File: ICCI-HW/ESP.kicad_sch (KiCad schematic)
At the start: 45 parts, among them J501 JTAG, SW501 SW_BOOT, SW502 SW_RST, SW503 SW_LOG_SD_EN, SW504 SW_RST_PROV, SW505 SW_RGB_CHRG, SW506 SW_SLEEP, U501 ESP32-WROVER-IE/E, U502 SX1503I091TRT

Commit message: hw: updates
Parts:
- added C512, C513, C516: 4.7u, Capacitor_SMD:C_0603_1608Metric, symbol Device:C
- added C514, C515, C517: 100n, Capacitor_SMD:C_0603_1608Metric, symbol Device:C
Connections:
- net +3V3: now also C512.1, C513.1, C514.1, C515.1, C516.1, C517.1
- net GND: now also C512.2, C513.2, C514.2, C515.2, C516.2, C517.2

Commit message: hw: updates
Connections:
- net RXD: no longer R512.2, U501.34 (RXD0)
- net TXD: no longer R511.1, U501.35 (TXD0)
- new net RXDR: R512.2, U501.34 (RXD0)
- new net TXDR: R511.1, U501.35 (TXD0)
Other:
- note added: "BOOT"
- note added: "RST"
- note added: "VSPI_D"
- note added: "VSPI_Q"
- moved on the sheet: C502, C504, C507, C508, C509, D501, D502, R505, R506, R507, R511, R512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

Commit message: start layout
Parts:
- removed J501: JTAG, Connector_PinHeader_2.54mm:PinHeader_1x04_P2.54mm_Vertical, symbol Connector_Generic:Conn_01x04
- removed TP506: TP_CLK/TP, TestPoint:TestPoint_Plated_Hole_D2.0mm, symbol Connector:TestPoint
- added J501: JTAG, ICCI-LIB:JST_B6B-XH-A, symbol Connector:Conn_01x06_Male
- added JP501, JP502, JP503: SolderJumper_3_Bridged12, Jumper:SolderJumper-3_P1.3mm_Open_RoundedPad1.0x1.5mm_NumberLabels, symbol Jumper:SolderJumper_3_Bridged12
- TP501, TP502, TP503, TP504, TP505, TP507, TP508: footprint TestPoint:TestPoint_Plated_Hole_D2.0mm -> TestPoint:TestPoint_THTPad_D1.5mm_Drill0.7mm
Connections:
- net +3V3: now also J501.6 (Pin_6)
- net GND: now also J501.1 (Pin_1)
- net GPS_EXTINT: now also JP503.3 (B); no longer U502.20 (I/O[13])
- net GPS_TP: now also JP501.3 (B); no longer U502.23 (I/O[15])
- net TCK: now also J501.4 (Pin_4)
- net TDI: now also J501.2 (Pin_2)
- net TDO: now also J501.3 (Pin_3)
- net TMS: now also J501.5 (Pin_5)
- net ~{GPS_RESET}: now also JP502.3 (B); no longer U502.22 (I/O[14])
- new net: JP501.2 (C), U502.23 (I/O[15])
- new net: JP503.2 (C), U502.20 (I/O[13])
- new net: JP502.2 (C), U502.22 (I/O[14])
- new net RTC_CLKOUT: JP501.1 (A)
- new net ~{RTC_INT}: JP503.1 (A)
- new net ~{RTC_RST}: JP502.1 (A)
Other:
- note added: "Solder Jumpers Pos. 1-2 if RTC mounted, 3-2 if GPS mounted."
- moved on the sheet: TP503

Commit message: layout PCB V1.0
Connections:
- net ~{EXP_RESET} renamed ~{EXP_RST}
- net ~{GPS_RESET} renamed ~{GPS_RST}
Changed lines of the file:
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@@
     (title "ESP")
     (date "2022-07-14")
-    (rev "BETA")
+    (rev "1.0")
     (company "Simone Tollardo")
   )
@@
     (effects (font (size 1.27 1.27)) (justify left bottom))
   )
-  (label "~{EXP_RESET}" (at 212.725 62.865 180)
+  (label "~{EXP_RST}" (at 212.725 62.865 180)
     (effects (font (size 1.27 1.27)) (justify right bottom))
   )
@@
     (effects (font (size 1.27 1.27)) (justify right bottom))
   )
-  (label "~{EXP_RESET}" (at 172.466 59.69 180)
+  (label "~{EXP_RST}" (at 172.466 59.69 180)
     (effects (font (size 1.27 1.27)) (justify right bottom))
   )
@@
     (effects (font (size 1.27 1.27)) (justify right))
   )
-  (hierarchical_label "~{GPS_RESET}" (shape output) (at 222.885 29.21 180)
+  (hierarchical_label "~{GPS_RST}" (shape output) (at 222.885 29.21 180)
     (effects (font (size 1.27 1.27)) (justify right))
   )

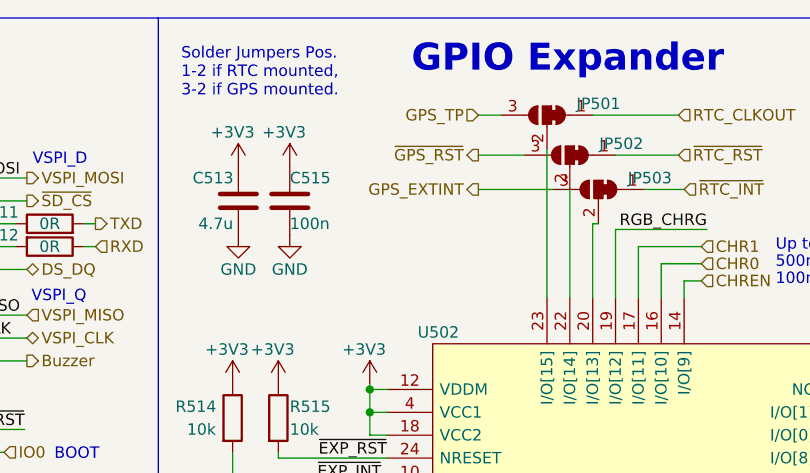
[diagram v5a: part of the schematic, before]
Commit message: hw: fix missing contact from SYS to SYSA on MAX77960
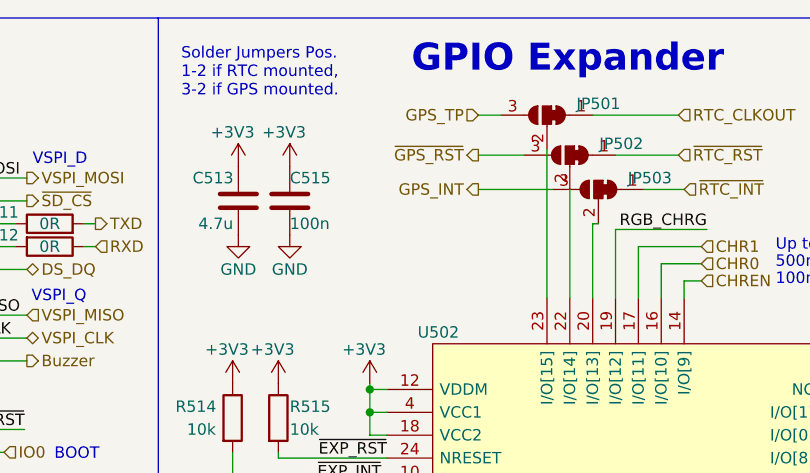
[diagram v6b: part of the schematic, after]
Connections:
- net GPS_EXTINT renamed GPS_INT
